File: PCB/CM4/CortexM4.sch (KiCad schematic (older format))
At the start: 10 parts, among them U1 STM32F105RC, X1 ABM8G

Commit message: altimeter caps
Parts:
- added C13, C14: 10uF, 0805, symbol C
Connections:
- net +3.3V: now also C13.1, C14.1
- net GND: now also C13.2, C14.2
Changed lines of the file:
@@
-EESchema Schematic File Version 2  date Sun 04 Nov 2012 06:51:49 PM COT
+EESchema Schematic File Version 2  date Sun 04 Nov 2012 07:09:00 PM COT
 LIBS:power
 LIBS:device
@@
 Sheet 3 3
 Title ""
-Date "4 nov 2012"
+Date "5 nov 2012"
 Rev ""
 Comp ""
@@
 $EndComp
 $Comp
-L GND #PWR011
+L GND #PWR21
 U 1 1 50959F93
 P 6000 1350
-F 0 "#PWR011" H 6000 1350 30  0001 C CNN
+F 0 "#PWR21" H 6000 1350 30  0001 C CNN
 F 1 "GND" H 6000 1280 30  0001 C CNN
 	1    6000 1350
@@
 $EndComp
 $Comp
-L +3.3V #PWR012
+L +3.3V #PWR18
 U 1 1 5095A033
 P 4000 1050
-F 0 "#PWR012" H 4000 1010 30  0001 C CNN
+F 0 "#PWR18" H 4000 1010 30  0001 C CNN
 F 1 "+3.3V" H 4000 1160 30  0000 C CNN
 	1    4000 1050
@@
 $EndComp
 $Comp
-L +3.3V #PWR013
+L +3.3V #PWR20
 U 1 1 5095A042
 P 6000 750
-F 0 "#PWR013" H 6000 710 30  0001 C CNN
+F 0 "#PWR20" H 6000 710 30  0001 C CNN
 F 1 "+3.3V" H 6000 860 30  0000 C CNN
 	1    6000 750
@@
 Connection ~ 1350 2250
 $Comp
-L GND #PWR014
+L GND #PWR15
 U 1 1 5095A327
 P 1250 2700
-F 0 "#PWR014" H 1250 2700 30  0001 C CNN
+F 0 "#PWR15" H 1250 2700 30  0001 C CNN
 F 1 "GND" H 1250 2630 30  0001 C CNN
 	1    1250 2700
@@
 	1    0    0    -1
 $EndComp
-Wire Wire Line
-	7250 800  7250 850
 Connection ~ 6850 800
-Wire Wire Line
-	7250 1300 7250 1250
 Connection ~ 6850 1300
 Wire Wire Line
@@
 	2800 6100 2400 6100
 $Comp
-L GND #PWR015
+L GND #PWR19
 U 1 1 5095B7B5
 P 4100 7400
-F 0 "#PWR015" H 4100 7400 30  0001 C CNN
+F 0 "#PWR19" H 4100 7400 30  0001 C CNN
 F 1 "GND" H 4100 7330 30  0001 C CNN
 	1    4100 7400
@@
 	1650 4750 2800 4750
 $Comp
-L +3.3V #PWR016
+L +3.3V #PWR16
 U 1 1 5095EF23
 P 1850 3950
-F 0 "#PWR016" H 1850 3910 30  0001 C CNN
+F 0 "#PWR16" H 1850 3910 30  0001 C CNN
 F 1 "+3.3V" H 1850 4060 30  0000 C CNN
 	1    1850 3950
@@
 $EndComp
 $Comp
-L +3.3V #PWR017
+L +3.3V #PWR17
 U 1 1 5095EF45
 P 2150 3950
-F 0 "#PWR017" H 2150 3910 30  0001 C CNN
+F 0 "#PWR17" H 2150 3910 30  0001 C CNN
 F 1 "+3.3V" H 2150 4060 30  0000 C CNN
 	1    2150 3950
@@
 	2150 4550 2150 4750
 Connection ~ 2150 4750
+Wire Wire Line
+	6450 800  8150 800
+Wire Wire Line
+	6450 1300 7700 1300
+$Comp
+L C C13
+U 1 1 509705B9
+P 7700 1050
+F 0 "C13" H 7750 1150 50  0000 L CNN
+F 1 "10uF" H 7750 950 50  0000 L CNN
+F 2 "0805" H 7700 1050 60  0001 C CNN
+	1    7700 1050
+	1    0    0    -1
+$EndComp
+Wire Wire Line
+	7700 800  7700 850
+Wire Wire Line
+	7700 1300 7700 1250
+Wire Wire Line
+	6900 1300 8150 1300
+$Comp
+L C C14
+U 1 1 509705CE
+P 8150 1050
+F 0 "C14" H 8200 1150 50  0000 L CNN
+F 1 "10uF" H 8200 950 50  0000 L CNN
+F 2 "0805" H 8150 1050 60  0001 C CNN
+	1    8150 1050
+	1    0    0    -1
+$EndComp
+Wire Wire Line
+	8150 800  8150 850
+Wire Wire Line
+	8150 1300 8150 1250
+Connection ~ 7700 800
+Wire Wire Line
+	7250 800  7250 850
+Connection ~ 7250 800
+Wire Wire Line
+	7250 1300 7250 1250
+Connection ~ 7250 1300
+Connection ~ 7700 1300
 $EndSCHEMATC

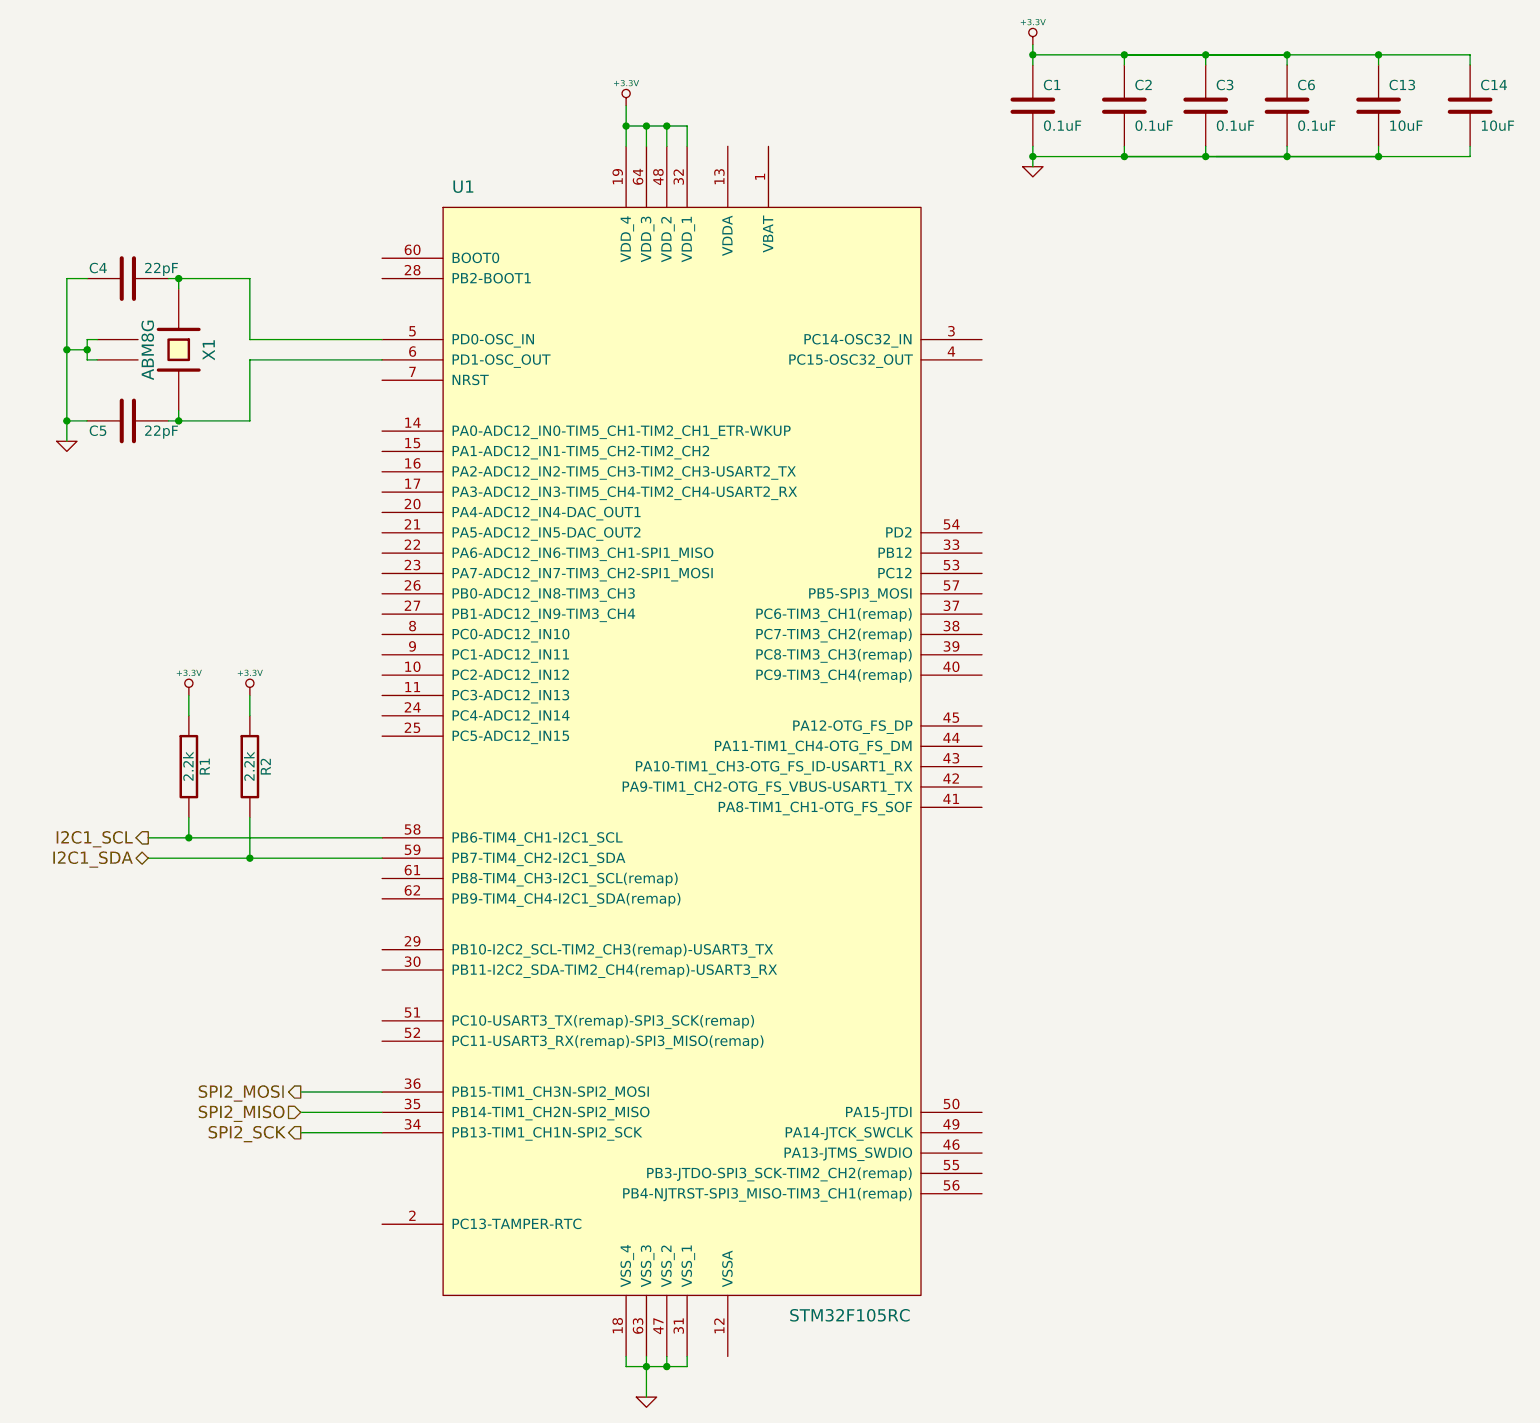
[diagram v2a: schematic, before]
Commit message: changing SPI Cortex M4 portd
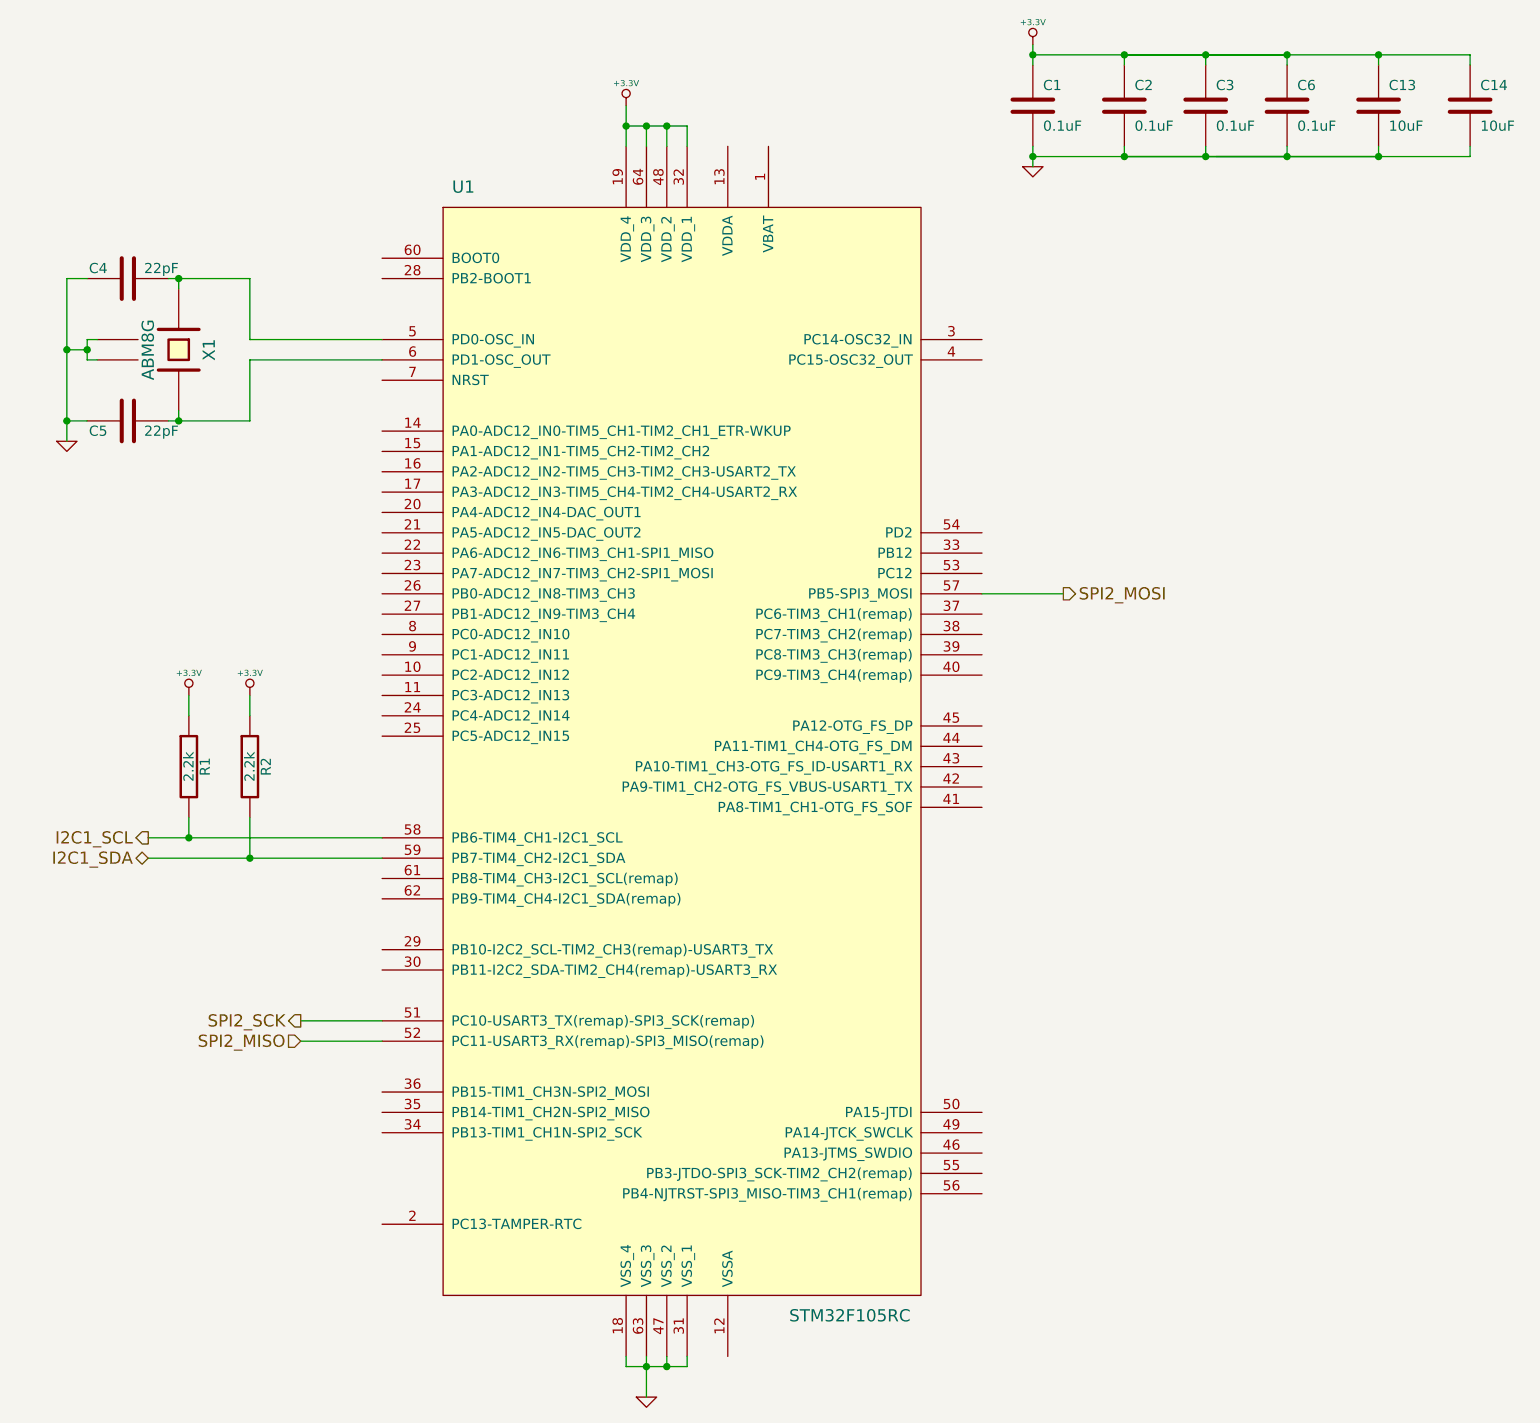
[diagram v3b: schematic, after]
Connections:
- net SPI2_MISO: now also U1.52 (PC11-USART3_RX(remap)-SPI3_MISO(remap)); no longer U1.35 (PB14-TIM1_CH2N-SPI2_MISO)
- net SPI2_MOSI: now also U1.57 (PB5-SPI3_MOSI); no longer U1.36 (PB15-TIM1_CH3N-SPI2_MOSI)
- net SPI2_SCK: now also U1.51 (PC10-USART3_TX(remap)-SPI3_SCK(remap)); no longer U1.34 (PB13-TIM1_CH1N-SPI2_SCK)
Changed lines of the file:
@@
-EESchema Schematic File Version 2  date Sun 04 Nov 2012 07:09:00 PM COT
+EESchema Schematic File Version 2  date Sun 04 Nov 2012 10:48:55 PM COT
 LIBS:power
 LIBS:device
@@
 LIBS:bmp085
 LIBS:HackBo_DroneCore_CM4-cache
-EELAYER 25  0
+EELAYER 27 0
 EELAYER END
 $Descr A4 11693 8268
@@
 $EndComp
 $Comp
-L GND #PWR21
+L GND #PWR015
 U 1 1 50959F93
 P 6000 1350
-F 0 "#PWR21" H 6000 1350 30  0001 C CNN
+F 0 "#PWR015" H 6000 1350 30  0001 C CNN
 F 1 "GND" H 6000 1280 30  0001 C CNN
 	1    6000 1350
@@
 $EndComp
 $Comp
-L +3.3V #PWR18
+L +3.3V #PWR016
 U 1 1 5095A033
 P 4000 1050
-F 0 "#PWR18" H 4000 1010 30  0001 C CNN
+F 0 "#PWR016" H 4000 1010 30  0001 C CNN
 F 1 "+3.3V" H 4000 1160 30  0000 C CNN
 	1    4000 1050
@@
 $EndComp
 $Comp
-L +3.3V #PWR20
+L +3.3V #PWR017
 U 1 1 5095A042
 P 6000 750
-F 0 "#PWR20" H 6000 710 30  0001 C CNN
+F 0 "#PWR017" H 6000 710 30  0001 C CNN
 F 1 "+3.3V" H 6000 860 30  0000 C CNN
 	1    6000 750
@@
 Connection ~ 1350 2250
 $Comp
-L GND #PWR15
+L GND #PWR018
 U 1 1 5095A327
 P 1250 2700
-F 0 "#PWR15" H 1250 2700 30  0001 C CNN
+F 0 "#PWR018" H 1250 2700 30  0001 C CNN
 F 1 "GND" H 1250 2630 30  0001 C CNN
 	1    1250 2700
@@
 Wire Wire Line
 	1750 1900 2150 1900
-Text HLabel 2400 5900 0    60   Output ~ 0
+Text HLabel 6150 3450 2    60   Output ~ 0
 SPI2_MOSI
-Text HLabel 2400 6000 0    60   Input ~ 0
+Text HLabel 2400 5650 0    60   Input ~ 0
 SPI2_MISO
-Text HLabel 2400 6100 0    60   Output ~ 0
+Text HLabel 2400 5550 0    60   Output ~ 0
 SPI2_SCK
 Wire Wire Line
-	2400 5900 2800 5900
-Wire Wire Line
-	2400 6000 2800 6000
-Wire Wire Line
-	2800 6100 2400 6100
-$Comp
-L GND #PWR19
+	6150 3450 5750 3450
+Wire Wire Line
+	2400 5650 2800 5650
+Wire Wire Line
+	2800 5550 2400 5550
+$Comp
+L GND #PWR019
 U 1 1 5095B7B5
 P 4100 7400
-F 0 "#PWR19" H 4100 7400 30  0001 C CNN
+F 0 "#PWR019" H 4100 7400 30  0001 C CNN
 F 1 "GND" H 4100 7330 30  0001 C CNN
 	1    4100 7400
@@
 	1650 4750 2800 4750
 $Comp
-L +3.3V #PWR16
+L +3.3V #PWR020
 U 1 1 5095EF23
 P 1850 3950
-F 0 "#PWR16" H 1850 3910 30  0001 C CNN
+F 0 "#PWR020" H 1850 3910 30  0001 C CNN
 F 1 "+3.3V" H 1850 4060 30  0000 C CNN
 	1    1850 3950
@@
 $EndComp
 $Comp
-L +3.3V #PWR17
+L +3.3V #PWR021
 U 1 1 5095EF45
 P 2150 3950
-F 0 "#PWR17" H 2150 3910 30  0001 C CNN
+F 0 "#PWR021" H 2150 3910 30  0001 C CNN
 F 1 "+3.3V" H 2150 4060 30  0000 C CNN
 	1    2150 3950

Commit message: Connection to connectors
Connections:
- net pwm_01: now reaches U1.14 (PA0-ADC12_IN0-TIM5_CH1-TIM2_CH1_ETR-WKUP)
- net pwm_02: now reaches U1.15 (PA1-ADC12_IN1-TIM5_CH2-TIM2_CH2)
- net pwm_03: now reaches U1.16 (PA2-ADC12_IN2-TIM5_CH3-TIM2_CH3-USART2_TX)
- net pwm_04: now reaches U1.17 (PA3-ADC12_IN3-TIM5_CH4-TIM2_CH4-USART2_RX)
- net pwm_05: now reaches U1.20 (PA4-ADC12_IN4-DAC_OUT1)
- net pwm_06: now reaches U1.21 (PA5-ADC12_IN5-DAC_OUT2)
- net pwm_07: now reaches U1.22 (PA6-ADC12_IN6-TIM3_CH1-SPI1_MISO)
- net pwm_08: now reaches U1.23 (PA7-ADC12_IN7-TIM3_CH2-SPI1_MOSI)
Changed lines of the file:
@@
-EESchema Schematic File Version 2  date Mon 05 Nov 2012 06:52:04 AM COT
+EESchema Schematic File Version 2  date Mon 05 Nov 2012 10:11:56 PM EST
 LIBS:power
 LIBS:device
@@
 LIBS:bmp085
 LIBS:mpu6000
+LIBS:ap1115a
 LIBS:HackBo_DroneCore_CM4-cache
 EELAYER 27 0
@@
 $Descr A4 11693 8268
 encoding utf-8
-Sheet 3 3
+Sheet 3 4
 Title ""
-Date "5 nov 2012"
+Date "6 nov 2012"
 Rev ""
 Comp ""
@@
 Connection ~ 7250 1300
 Connection ~ 7700 1300
+Text HLabel 2650 2650 0    60   Output ~ 0
+pwm_01
+Wire Wire Line
+	2650 2650 2800 2650
+Text HLabel 2650 2750 0    60   Output ~ 0
+pwm_02
+Wire Wire Line
+	2650 2750 2800 2750
+Text HLabel 2650 2850 0    60   Output ~ 0
+pwm_03
+Wire Wire Line
+	2650 2850 2800 2850
+Text HLabel 2650 2950 0    60   Output ~ 0
+pwm_04
+Wire Wire Line
+	2650 2950 2800 2950
+Text HLabel 2650 3050 0    60   Output ~ 0
+pwm_05
+Wire Wire Line
+	2650 3050 2800 3050
+Text HLabel 2650 3150 0    60   Output ~ 0
+pwm_06
+Wire Wire Line
+	2650 3150 2800 3150
+Text HLabel 2650 3250 0    60   Output ~ 0
+pwm_07
+Wire Wire Line
+	2650 3250 2800 3250
+Text HLabel 2650 3350 0    60   Output ~ 0
+pwm_08
+Wire Wire Line
+	2650 3350 2800 3350
 $EndSCHEMATC

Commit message: 5v power  and reset
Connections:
- net RESET: now reaches U1.7 (NRST)
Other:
- moved on the sheet: C4, C5, X1
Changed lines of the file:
@@
-EESchema Schematic File Version 2  date Mon 05 Nov 2012 10:11:56 PM EST
+EESchema Schematic File Version 2  date Tue 06 Nov 2012 07:35:26 PM EST
 LIBS:power
 LIBS:device
@@
 Sheet 3 4
 Title ""
-Date "6 nov 2012"
+Date "7 nov 2012"
 Rev ""
 Comp ""
@@
 $EndComp
 $Comp
-L GND #PWR25
+L GND #PWR21
 U 1 1 50959F93
 P 6000 1350
-F 0 "#PWR25" H 6000 1350 30  0001 C CNN
+F 0 "#PWR21" H 6000 1350 30  0001 C CNN
 F 1 "GND" H 6000 1280 30  0001 C CNN
 	1    6000 1350
@@
 $EndComp
 $Comp
-L +3.3V #PWR22
+L +3.3V #PWR20
 U 1 1 5095A033
 P 4000 1050
-F 0 "#PWR22" H 4000 1010 30  0001 C CNN
+F 0 "#PWR20" H 4000 1010 30  0001 C CNN
 F 1 "+3.3V" H 4000 1160 30  0000 C CNN
 	1    4000 1050
@@
 $EndComp
 $Comp
-L +3.3V #PWR24
+L +3.3V #PWR19
 U 1 1 5095A042
 P 6000 750
-F 0 "#PWR24" H 6000 710 30  0001 C CNN
+F 0 "#PWR19" H 6000 710 30  0001 C CNN
 F 1 "+3.3V" H 6000 860 30  0000 C CNN
 	1    6000 750
@@
 L ABM8G X1
 U 1 1 5095A15D
-P 1800 2250
-F 0 "X1" H 1800 2400 60  0000 C CNN
-F 1 "ABM8G" H 1800 2100 60  0000 C CNN
-F 2 "ABM8G" H 1800 2250 60  0001 C CNN
-	1    1800 2250
+P 1600 1950
+F 0 "X1" H 1600 2100 60  0000 C CNN
+F 1 "ABM8G" H 1600 1800 60  0000 C CNN
+F 2 "ABM8G" H 1600 1950 60  0001 C CNN
+	1    1600 1950
 	0    1    1    0
 $EndComp
@@
 L C C4
 U 1 1 5095A176
-P 1550 1900
-F 0 "C4" V 1600 2000 50  0000 L CNN
-F 1 "22pF" V 1600 1650 50  0000 L CNN
-F 2 "0603" H 1550 1900 60  0001 C CNN
-	1    1550 1900
+P 1350 1600
+F 0 "C4" V 1400 1700 50  0000 L CNN
+F 1 "22pF" V 1400 1350 50  0000 L CNN
+F 2 "0603" H 1350 1600 60  0001 C CNN
+	1    1350 1600
 	0    -1   -1   0
 $EndComp
@@
 L C C5
 U 1 1 5095A1AA
-P 1550 2600
-F 0 "C5" V 1500 2700 50  0000 L CNN
-F 1 "22pF" V 1500 2350 50  0000 L CNN
-F 2 "0603" H 1550 2600 60  0001 C CNN
-	1    1550 2600
+P 1350 2300
+F 0 "C5" V 1300 2400 50  0000 L CNN
+F 1 "22pF" V 1300 2050 50  0000 L CNN
+F 2 "0603" H 1350 2300 60  0001 C CNN
+	1    1350 2300
 	0    -1   -1   0
 $EndComp
@@
 	2150 2200 2800 2200
 Wire Wire Line
-	1800 1950 1800 1900
-Connection ~ 1800 1900
-Wire Wire Line
-	2150 2300 2800 2300
-Wire Wire Line
-	1800 2550 1800 2600
-Connection ~ 1800 2600
-Wire Wire Line
-	1400 2300 1350 2300
-Wire Wire Line
-	1350 2300 1350 2200
-Wire Wire Line
-	1350 2200 1400 2200
-Wire Wire Line
-	1350 1900 1250 1900
-Wire Wire Line
-	1250 1900 1250 2700
-Wire Wire Line
-	1350 2600 1250 2600
-Connection ~ 1250 2600
-Wire Wire Line
-	1350 2250 1250 2250
-Connection ~ 1250 2250
-Connection ~ 1350 2250
-$Comp
-L GND #PWR19
+	1600 1650 1600 1600
+Connection ~ 1600 1600
+Wire Wire Line
+	1550 2300 2800 2300
+Wire Wire Line
+	1600 2250 1600 2300
+Connection ~ 1600 2300
+Wire Wire Line
+	1200 2000 1150 2000
+Wire Wire Line
+	1150 2000 1150 1900
+Wire Wire Line
+	1150 1900 1200 1900
+Wire Wire Line
+	1150 1600 1050 1600
+Wire Wire Line
+	1050 1600 1050 2400
+Wire Wire Line
+	1150 2300 1050 2300
+Connection ~ 1050 2300
+Wire Wire Line
+	1150 1950 1050 1950
+Connection ~ 1050 1950
+Connection ~ 1150 1950
+$Comp
+L GND #PWR22
 U 1 1 5095A327
-P 1250 2700
-F 0 "#PWR19" H 1250 2700 30  0001 C CNN
-F 1 "GND" H 1250 2630 30  0001 C CNN
-	1    1250 2700
+P 1050 2400
+F 0 "#PWR22" H 1050 2400 30  0001 C CNN
+F 1 "GND" H 1050 2330 30  0001 C CNN
+	1    1050 2400
 	1    0    0    -1
 $EndComp
@@
 Connection ~ 6850 1300
 Wire Wire Line
-	1750 2600 2150 2600
-Wire Wire Line
-	2150 2600 2150 2300
-Wire Wire Line
-	2150 1900 2150 2200
-Wire Wire Line
-	1750 1900 2150 1900
+	2150 1600 2150 2200
+Wire Wire Line
+	1550 1600 2150 1600
 Text HLabel 6150 3450 2    60   Output ~ 0
 SPI2_MOSI
@@
 	2800 5550 2400 5550
 $Comp
-L GND #PWR23
+L GND #PWR25
 U 1 1 5095B7B5
 P 4100 7400
-F 0 "#PWR23" H 4100 7400 30  0001 C CNN
+F 0 "#PWR25" H 4100 7400 30  0001 C CNN
 F 1 "GND" H 4100 7330 30  0001 C CNN
 	1    4100 7400
@@
 	1650 4750 2800 4750
 $Comp
-L +3.3V #PWR20
+L +3.3V #PWR23
 U 1 1 5095EF23
 P 1850 3950
-F 0 "#PWR20" H 1850 3910 30  0001 C CNN
+F 0 "#PWR23" H 1850 3910 30  0001 C CNN
 F 1 "+3.3V" H 1850 4060 30  0000 C CNN
 	1    1850 3950
@@
 $EndComp
 $Comp
-L +3.3V #PWR21
+L +3.3V #PWR24
 U 1 1 5095EF45
 P 2150 3950
-F 0 "#PWR21" H 2150 3910 30  0001 C CNN
+F 0 "#PWR24" H 2150 3910 30  0001 C CNN
 F 1 "+3.3V" H 2150 4060 30  0000 C CNN
 	1    2150 3950
@@
 Wire Wire Line
 	2650 3350 2800 3350
+Text HLabel 2650 2400 0    60   Input ~ 0
+RESET
+Wire Wire Line
+	2650 2400 2800 2400
 $EndSCHEMATC
